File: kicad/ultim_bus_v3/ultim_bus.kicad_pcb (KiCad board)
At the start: 2 copper layers, 180.3 x 55.9 mm, 97 parts, among them M10 MouseBite, M11 MouseBite, M13 MouseBite, M16 MouseBite, M17 MouseBite, M18 MouseBite, M2 MouseBite, M3 MouseBite, M4 MouseBite, M6 MouseBite, M9 MouseBite, P1 CONN_1, P10 CONN_1, P11 CONN_1, P12 CONN_1, P14 CONN_1, P15 CONN_1, P16 CONN_1, P17 CONN_1, P18 CONN_1, P19 CONN_1, P2 CONN_1, P20 CONN_1, P21 CONN_1, P22 CONN_1, P23 CONN_1, P24 CONN_1, P25 CONN_1, P27 CONN_1, P28 CONN_1, P29 CONN_1, P3 CONN_1, P30 CONN_1, P31 CONN_1, P32 CONN_1, P33 CONN_1, P34 CONN_1, P35 CONN_1, P36 CONN_1, P37 CONN_1, P38 CONN_1, P4 CONN_1, P40 CONN_1, P41 CONN_1, P42 CONN_1, P43 CONN_1, P44 CONN_1, P45 CONN_1, P46 CONN_1, P47 CONN_1, P48 CONN_1, P49 CONN_1, P5 CONN_1, P50 CONN_1, P51 CONN_1, P6 CONN_1, P7 CONN_1, P8 CONN_1, P9 CONN_1

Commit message: corrections and cleanup
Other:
- board size 180.3 x 55.9 mm -> 177.8 x 55.9 mm

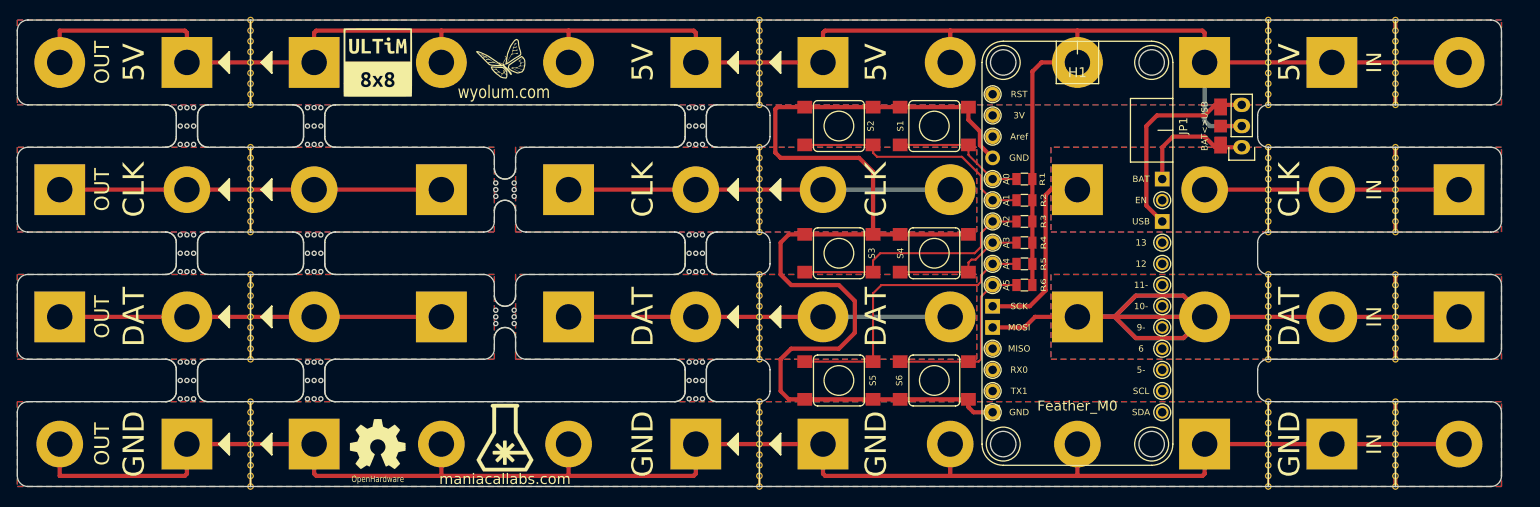
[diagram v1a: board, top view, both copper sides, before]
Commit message: Bus Bar PCB added El. Cap, removed short to GND
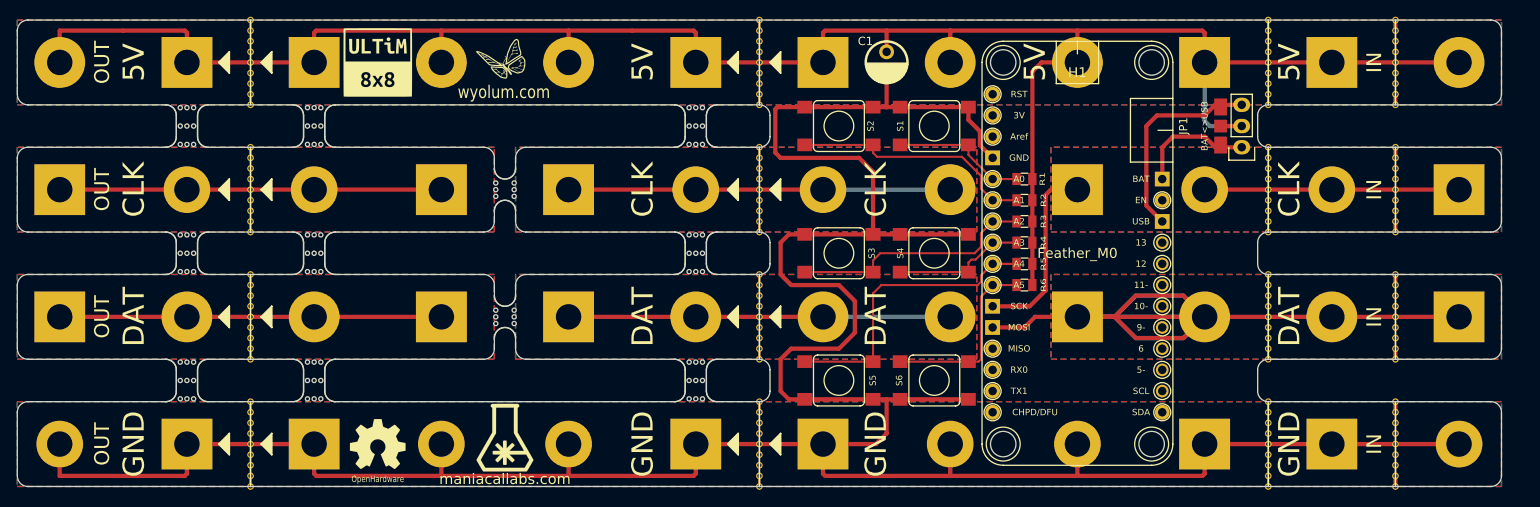
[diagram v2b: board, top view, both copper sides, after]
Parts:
- added C1: 470uF 10V, ultim_bus:cap_pol_rad3, F.Cu at (132.1, 30.5)
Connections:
- H1 pad 28: /GND -> (no net)
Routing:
- net /GND: track 354.8 -> 367.1 mm
- net /5V: track 260.8 -> 263.4 mm
